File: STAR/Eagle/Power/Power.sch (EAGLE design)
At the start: 46 parts, among them J1 J30J-25, U1 LMR16020, U2 LMR16020, U3 LMR16020

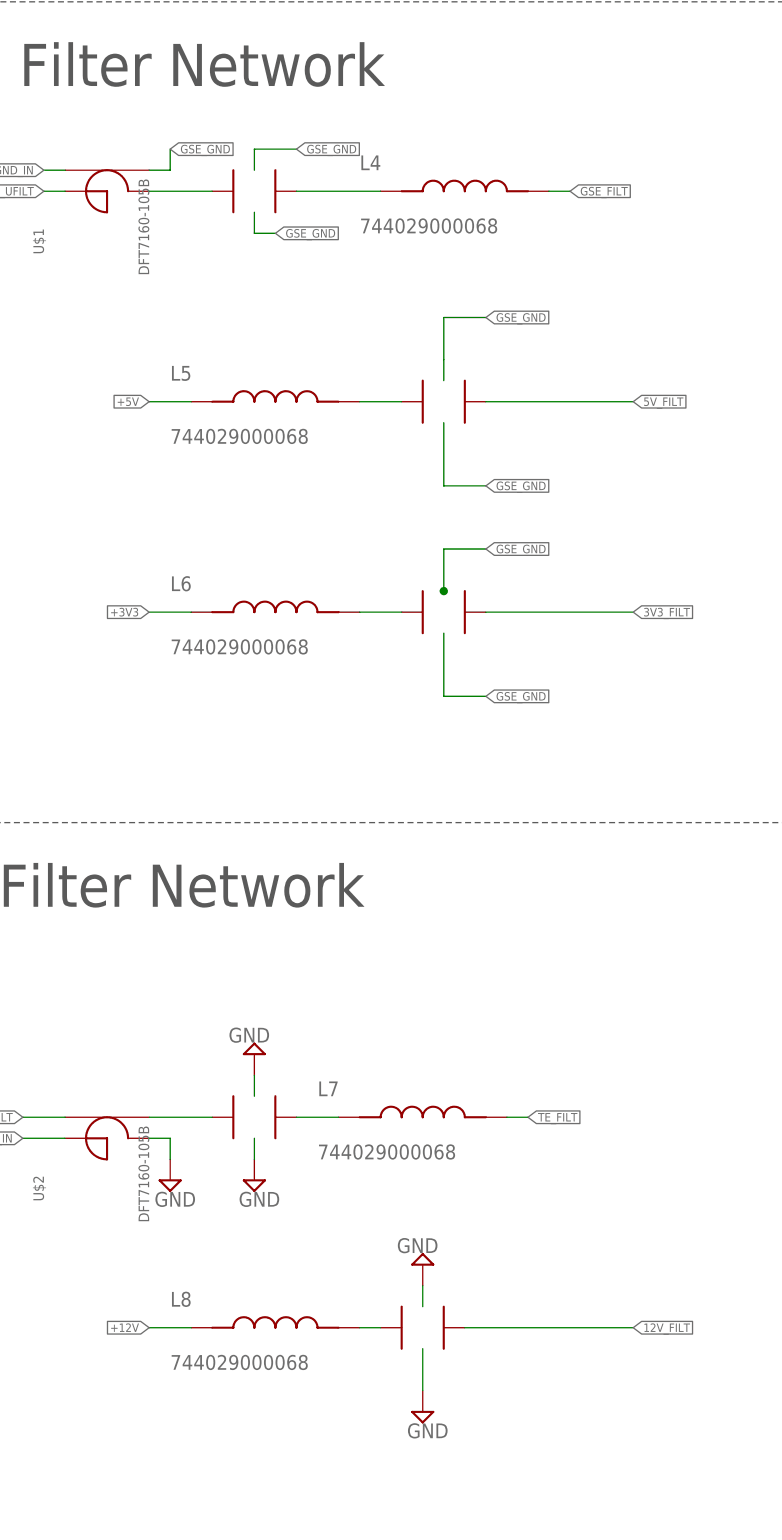
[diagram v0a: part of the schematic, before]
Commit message: reoriented capacitors on power board
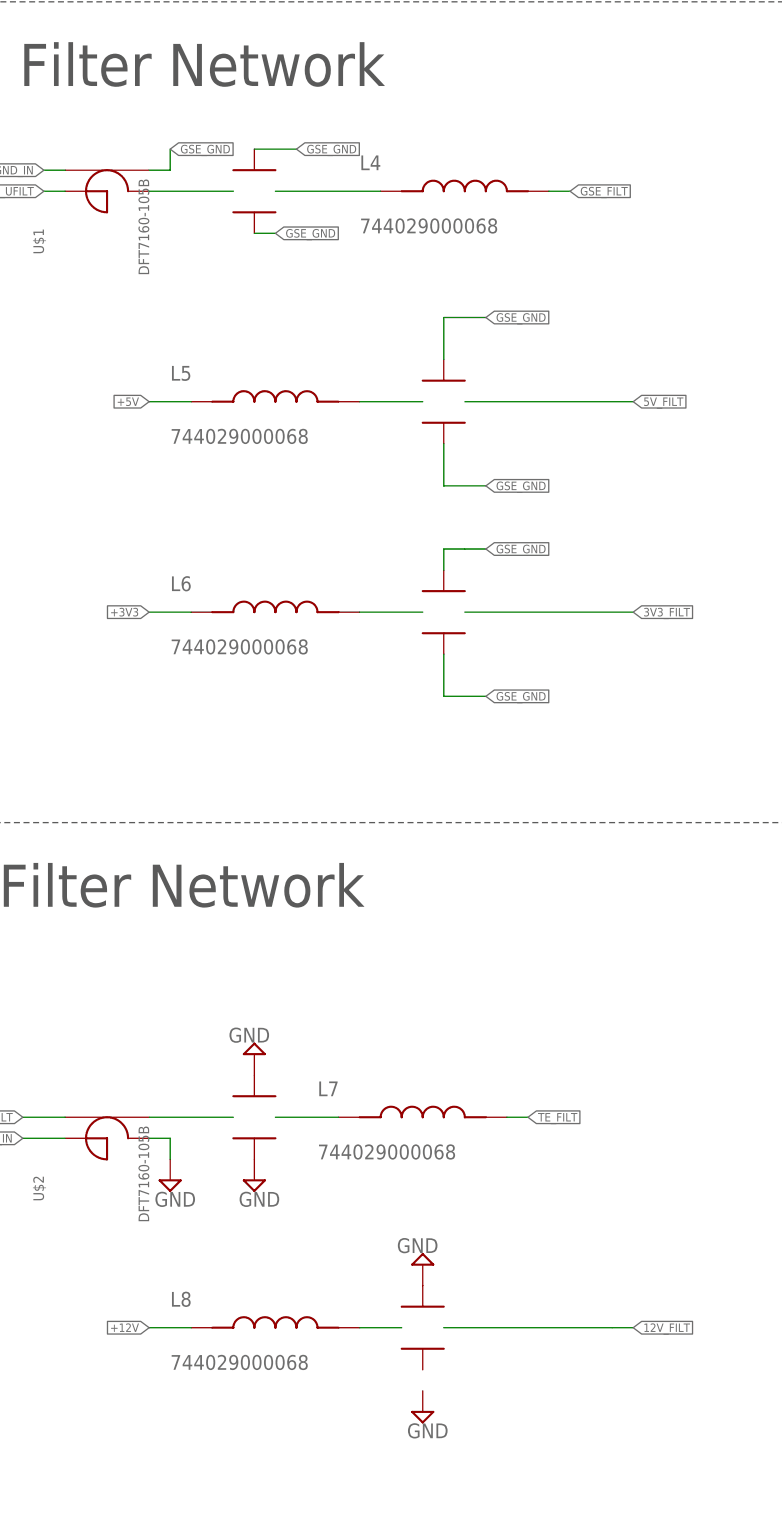
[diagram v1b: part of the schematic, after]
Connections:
- net 12V_FILT: now also U$7.P$3; no longer U$7.P$2
- net 3V3_FILT: now also U$5.P$3; no longer U$5.P$2
- net 5V_FILT: now also U$4.P$3; no longer U$4.P$1
- net GND: now also U$6.P$1, U$6.P$2; no longer U$6.P$3, U$6.P$4, U$7.P$3, U$7.P$4
- net GSE_GND: now also U$3.P$1, U$3.P$2, U$4.P$1, U$4.P$2, U$5.P$1, U$5.P$2; no longer U$3.P$3, U$3.P$4, U$4.P$3, U$4.P$4, U$5.P$3, U$5.P$4
- net N$28: now also U$1.P$2, U$3.P$3; no longer L4.P$1, U$3.P$1
- net N$29: now also U$6.P$4; no longer U$6.P$1
- net N$31: now also L4.P$1, U$3.P$4; no longer U$1.P$2, U$3.P$2
- net N$32: now also U$4.P$4; no longer U$4.P$2
- net N$33: now also U$5.P$4; no longer U$5.P$1
- net N$34: now also U$6.P$3; no longer U$6.P$2
- net N$35: now also U$7.P$4; no longer U$7.P$1
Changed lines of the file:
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@@
 <instance part="FRAME1" gate="G$1" x="38.1" y="63.5"/>
 <instance part="J1" gate="G$1" x="330.2" y="223.52"/>
-<instance part="U$3" gate="G$1" x="233.68" y="251.46" rot="R90"/>
-<instance part="U$4" gate="G$1" x="256.54" y="226.06" rot="R90"/>
-<instance part="U$5" gate="G$1" x="256.54" y="200.66" rot="R270"/>
-<instance part="U$6" gate="G$1" x="233.68" y="139.7" rot="R270"/>
-<instance part="U$7" gate="G$1" x="254" y="114.3" rot="R270"/>
+<instance part="U$3" gate="G$1" x="233.68" y="251.46" rot="R180"/>
+<instance part="U$4" gate="G$1" x="256.54" y="226.06"/>
+<instance part="U$5" gate="G$1" x="256.54" y="200.66"/>
+<instance part="U$6" gate="G$1" x="233.68" y="139.7"/>
+<instance part="U$7" gate="G$1" x="254" y="114.3"/>
 <instance part="SUPPLY2" gate="GND" x="233.68" y="147.32" rot="R180"/>
 <instance part="SUPPLY3" gate="GND" x="254" y="121.92" rot="R180"/>
@@
 </segment>
 <segment>
-<pinref part="SUPPLY33" gate="GND" pin="GND"/>
-<pinref part="U$6" gate="G$1" pin="P$3"/>
-<wire x1="233.68" y1="137.16" x2="233.68" y2="134.62" width="0.1524" layer="91"/>
-</segment>
-<segment>
-<pinref part="U$6" gate="G$1" pin="P$4"/>
-<wire x1="233.68" y1="142.24" x2="233.68" y2="144.78" width="0.1524" layer="91"/>
-<pinref part="SUPPLY2" gate="GND" pin="GND"/>
-</segment>
-<segment>
-<pinref part="SUPPLY34" gate="GND" pin="GND"/>
-<pinref part="U$7" gate="G$1" pin="P$3"/>
-<wire x1="254" y1="106.68" x2="254" y2="111.76" width="0.1524" layer="91"/>
-</segment>
-<segment>
-<pinref part="U$7" gate="G$1" pin="P$4"/>
-<wire x1="254" y1="116.84" x2="254" y2="119.38" width="0.1524" layer="91"/>
-<pinref part="SUPPLY3" gate="GND" pin="GND"/>
-</segment>
-<segment>
 <pinref part="U$2" gate="G$1" pin="P$2"/>
 <wire x1="220.98" y1="137.16" x2="223.52" y2="137.16" width="0.1524" layer="91"/>
@@
 <wire x1="322.58" y1="223.52" x2="325.12" y2="223.52" width="0.1524" layer="91"/>
 <label x="322.58" y="223.52" size="1.016" layer="95" rot="R180" xref="yes"/>
+</segment>
+<segment>
+<pinref part="SUPPLY33" gate="GND" pin="GND"/>
+<pinref part="U$6" gate="G$1" pin="P$1"/>
+</segment>
+<segment>
+<pinref part="SUPPLY2" gate="GND" pin="GND"/>
+<pinref part="U$6" gate="G$1" pin="P$2"/>
 </segment>
 </net>
@@
 <segment>
 <label x="279.4" y="226.06" size="1.016" layer="95" xref="yes"/>
-<pinref part="U$4" gate="G$1" pin="P$1"/>
-<wire x1="261.62" y1="226.06" x2="279.4" y2="226.06" width="0.1524" layer="91"/>
+<pinref part="U$4" gate="G$1" pin="P$3"/>
+<wire x1="259.08" y1="226.06" x2="279.4" y2="226.06" width="0.1524" layer="91"/>
 </segment>
 <segment>
@@
 <net name="3V3_FILT" class="0">
 <segment>
-<wire x1="261.62" y1="200.66" x2="279.4" y2="200.66" width="0.1524" layer="91"/>
 <label x="279.4" y="200.66" size="1.016" layer="95" xref="yes"/>
-<pinref part="U$5" gate="G$1" pin="P$2"/>
+<pinref part="U$5" gate="G$1" pin="P$3"/>
+<wire x1="279.4" y1="200.66" x2="259.08" y2="200.66" width="0.1524" layer="91"/>
 </segment>
 <segment>
@@
 <net name="12V_FILT" class="0">
 <segment>
-<wire x1="259.08" y1="114.3" x2="279.4" y2="114.3" width="0.1524" layer="91"/>
 <label x="279.4" y="114.3" size="1.016" layer="95" xref="yes"/>
-<pinref part="U$7" gate="G$1" pin="P$2"/>
+<pinref part="U$7" gate="G$1" pin="P$3"/>
+<wire x1="256.54" y1="114.3" x2="276.86" y2="114.3" width="0.1524" layer="91"/>
+<wire x1="276.86" y1="114.3" x2="279.4" y2="114.3" width="0.1524" layer="91"/>
 </segment>
 <segment>
@@
 </segment>
 </net>
-<net name="N$32" class="0">
-<segment>
-<pinref part="U$4" gate="G$1" pin="P$2"/>
-<pinref part="L5" gate="G$1" pin="P$2"/>
-<wire x1="251.46" y1="226.06" x2="246.38" y2="226.06" width="0.1524" layer="91"/>
-</segment>
-</net>
-<net name="N$33" class="0">
-<segment>
-<pinref part="L6" gate="G$1" pin="P$2"/>
-<pinref part="U$5" gate="G$1" pin="P$1"/>
-<wire x1="246.38" y1="200.66" x2="251.46" y2="200.66" width="0.1524" layer="91"/>
-</segment>
-</net>
-<net name="N$35" class="0">
-<segment>
-<pinref part="L8" gate="G$1" pin="P$2"/>
-<pinref part="U$7" gate="G$1" pin="P$1"/>
-<wire x1="246.38" y1="114.3" x2="248.92" y2="114.3" width="0.1524" layer="91"/>
-</segment>
-</net>
 <net name="GSE_GND_IN" class="0">
 <segment>
@@
 <label x="238.76" y="256.54" size="1.016" layer="95" xref="yes"/>
 <wire x1="233.68" y1="256.54" x2="238.76" y2="256.54" width="0.1524" layer="91"/>
-<pinref part="U$3" gate="G$1" pin="P$3"/>
-<wire x1="233.68" y1="256.54" x2="233.68" y2="254" width="0.1524" layer="91"/>
 <label x="223.52" y="256.54" size="1.016" layer="95" xref="yes"/>
+<pinref part="U$3" gate="G$1" pin="P$1"/>
 </segment>
 <segment>
 <label x="236.22" y="246.38" size="1.016" layer="95" xref="yes"/>
 <wire x1="233.68" y1="246.38" x2="236.22" y2="246.38" width="0.1524" layer="91"/>
-<pinref part="U$3" gate="G$1" pin="P$4"/>
-<wire x1="233.68" y1="246.38" x2="233.68" y2="248.92" width="0.1524" layer="91"/>
+<pinref part="U$3" gate="G$1" pin="P$2"/>
 </segment>
 <segment>
@@
 <wire x1="256.54" y1="236.22" x2="261.62" y2="236.22" width="0.1524" layer="91"/>
 <wire x1="256.54" y1="236.22" x2="256.54" y2="231.14" width="0.1524" layer="91"/>
-<wire x1="256.54" y1="228.6" x2="256.54" y2="231.14" width="0.1524" layer="91"/>
-<pinref part="U$4" gate="G$1" pin="P$3"/>
+<pinref part="U$4" gate="G$1" pin="P$2"/>
 </segment>
 <segment>
 <label x="261.62" y="215.9" size="1.016" layer="95" xref="yes"/>
 <wire x1="256.54" y1="215.9" x2="261.62" y2="215.9" width="0.1524" layer="91"/>
-<wire x1="256.54" y1="215.9" x2="256.54" y2="223.52" width="0.1524" layer="91"/>
 <label x="261.62" y="208.28" size="1.016" layer="95" xref="yes"/>
-<pinref part="U$4" gate="G$1" pin="P$4"/>
+<pinref part="U$4" gate="G$1" pin="P$1"/>
+<wire x1="256.54" y1="220.98" x2="256.54" y2="215.9" width="0.1524" layer="91"/>
 </segment>
 <segment>
 <label x="261.62" y="190.5" size="1.016" layer="95" xref="yes"/>
-<pinref part="U$5" gate="G$1" pin="P$3"/>
-<wire x1="256.54" y1="198.12" x2="256.54" y2="190.5" width="0.1524" layer="91"/>
 <wire x1="261.62" y1="190.5" x2="256.54" y2="190.5" width="0.1524" layer="91"/>
+<pinref part="U$5" gate="G$1" pin="P$1"/>
+<wire x1="256.54" y1="195.58" x2="256.54" y2="190.5" width="0.1524" layer="91"/>
 </segment>
 <segment>
@@
 </segment>
 <segment>
-<pinref part="U$5" gate="G$1" pin="P$4"/>
-<wire x1="256.54" y1="203.2" x2="256.54" y2="208.28" width="0.1524" layer="91"/>
-<wire x1="256.54" y1="208.28" x2="261.62" y2="208.28" width="0.1524" layer="91"/>
-<junction x="256.54" y="203.2"/>
+<pinref part="U$5" gate="G$1" pin="P$2"/>
+<wire x1="259.08" y1="208.28" x2="261.62" y2="208.28" width="0.1524" layer="91"/>
+<wire x1="259.08" y1="208.28" x2="256.54" y2="208.28" width="0.1524" layer="91"/>
+<wire x1="256.54" y1="208.28" x2="256.54" y2="205.74" width="0.1524" layer="91"/>
 </segment>
 <segment>
@@
 </segment>
 </net>
-<net name="N$28" class="0">
-<segment>
-<pinref part="U$3" gate="G$1" pin="P$1"/>
-<wire x1="238.76" y1="251.46" x2="248.92" y2="251.46" width="0.1524" layer="91"/>
-<pinref part="L4" gate="G$1" pin="P$1"/>
-</segment>
-</net>
-<net name="N$29" class="0">
-<segment>
-<pinref part="U$2" gate="G$1" pin="P$4"/>
-<pinref part="U$6" gate="G$1" pin="P$1"/>
-<wire x1="220.98" y1="139.7" x2="228.6" y2="139.7" width="0.1524" layer="91"/>
-</segment>
-</net>
-<net name="N$34" class="0">
-<segment>
-<pinref part="U$6" gate="G$1" pin="P$2"/>
-<pinref part="L7" gate="G$1" pin="P$1"/>
-<wire x1="238.76" y1="139.7" x2="243.84" y2="139.7" width="0.1524" layer="91"/>
-</segment>
-</net>
-<net name="N$31" class="0">
-<segment>
-<pinref part="U$1" gate="G$1" pin="P$2"/>
-<pinref part="U$3" gate="G$1" pin="P$2"/>
-<wire x1="220.98" y1="251.46" x2="228.6" y2="251.46" width="0.1524" layer="91"/>
-</segment>
-</net>
 <net name="N$38" class="0">
 <segment>
@@
 </segment>
 </net>
+<net name="N$28" class="0">
+<segment>
+<pinref part="U$1" gate="G$1" pin="P$2"/>
+<pinref part="U$3" gate="G$1" pin="P$3"/>
+<wire x1="220.98" y1="251.46" x2="231.14" y2="251.46" width="0.1524" layer="91"/>
+</segment>
+</net>
+<net name="N$31" class="0">
+<segment>
+<pinref part="U$3" gate="G$1" pin="P$4"/>
+<pinref part="L4" gate="G$1" pin="P$1"/>
+<wire x1="236.22" y1="251.46" x2="248.92" y2="251.46" width="0.1524" layer="91"/>
+</segment>
+</net>
+<net name="N$32" class="0">
+<segment>
+<pinref part="U$4" gate="G$1" pin="P$4"/>
+<pinref part="L5" gate="G$1" pin="P$2"/>
+<wire x1="254" y1="226.06" x2="246.38" y2="226.06" width="0.1524" layer="91"/>
+</segment>
+</net>
+<net name="N$33" class="0">
+<segment>
+<pinref part="U$5" gate="G$1" pin="P$4"/>
+<pinref part="L6" gate="G$1" pin="P$2"/>
+<wire x1="254" y1="200.66" x2="246.38" y2="200.66" width="0.1524" layer="91"/>
+</segment>
+</net>
+<net name="N$29" class="0">
+<segment>
+<pinref part="U$2" gate="G$1" pin="P$4"/>
+<pinref part="U$6" gate="G$1" pin="P$4"/>
+<wire x1="220.98" y1="139.7" x2="231.14" y2="139.7" width="0.1524" layer="91"/>
+</segment>
+</net>
+<net name="N$34" class="0">
+<segment>
+<pinref part="U$6" gate="G$1" pin="P$3"/>
+<pinref part="L7" gate="G$1" pin="P$1"/>
+<wire x1="236.22" y1="139.7" x2="243.84" y2="139.7" width="0.1524" layer="91"/>
+</segment>
+</net>
+<net name="N$35" class="0">
+<segment>
+<pinref part="L8" gate="G$1" pin="P$2"/>
+<pinref part="U$7" gate="G$1" pin="P$4"/>
+<wire x1="246.38" y1="114.3" x2="251.46" y2="114.3" width="0.1524" layer="91"/>
+</segment>
+</net>

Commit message: Fixed an air wire on the ground lines and a non-connection in the sketch
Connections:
- removed net N$38: U$1.P$4
- net GND: now also U$7.P$2
- net GSE_GND: now also U$1.P$4
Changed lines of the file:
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@@
 <?xml version="1.0" encoding="utf-8"?>
 <!DOCTYPE eagle SYSTEM "eagle.dtd">
-<eagle version="7.6.0">
+<eagle version="9.1.0">
 <drawing>
 <settings>
 <setting alwaysvectorfont="no"/>
+<setting keepoldvectorfont="yes"/>
 <setting verticaltext="up"/>
 </settings>
@@
 <pinref part="U$6" gate="G$1" pin="P$2"/>
 </segment>
+<segment>
+<pinref part="SUPPLY3" gate="GND" pin="GND"/>
+<pinref part="U$7" gate="G$1" pin="P$2"/>
+</segment>
 </net>
 <net name="+3V3" class="0">
@@
 <label x="238.76" y="256.54" size="1.016" layer="95" xref="yes"/>
 <wire x1="233.68" y1="256.54" x2="238.76" y2="256.54" width="0.1524" layer="91"/>
-<label x="223.52" y="256.54" size="1.016" layer="95" xref="yes"/>
 <pinref part="U$3" gate="G$1" pin="P$1"/>
 </segment>
@@
 <label x="261.62" y="215.9" size="1.016" layer="95" xref="yes"/>
 <wire x1="256.54" y1="215.9" x2="261.62" y2="215.9" width="0.1524" layer="91"/>
-<label x="261.62" y="208.28" size="1.016" layer="95" xref="yes"/>
 <pinref part="U$4" gate="G$1" pin="P$1"/>
 <wire x1="256.54" y1="220.98" x2="256.54" y2="215.9" width="0.1524" layer="91"/>
@@
 <wire x1="259.08" y1="208.28" x2="256.54" y2="208.28" width="0.1524" layer="91"/>
 <wire x1="256.54" y1="208.28" x2="256.54" y2="205.74" width="0.1524" layer="91"/>
+<label x="261.62" y="208.28" size="1.016" layer="95" xref="yes"/>
 </segment>
 <segment>
@@
 <label x="337.82" y="210.82" size="1.016" layer="95" xref="yes"/>
 </segment>
+<segment>
+<pinref part="U$1" gate="G$1" pin="P$4"/>
+<wire x1="220.98" y1="254" x2="223.52" y2="254" width="0.1524" layer="91"/>
+<wire x1="223.52" y1="254" x2="223.52" y2="256.54" width="0.1524" layer="91"/>
+<label x="223.52" y="256.54" size="1.016" layer="95" xref="yes"/>
+</segment>
 </net>
 <net name="TE_UFILT" class="0">
@@
 </segment>
 </net>
-<net name="N$38" class="0">
-<segment>
-<pinref part="U$1" gate="G$1" pin="P$4"/>
-<wire x1="220.98" y1="254" x2="223.52" y2="254" width="0.1524" layer="91"/>
-<wire x1="223.52" y1="254" x2="223.52" y2="256.54" width="0.1524" layer="91"/>
-</segment>
-</net>
